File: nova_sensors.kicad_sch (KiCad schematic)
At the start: 93 parts, among them J1 Conn_01x03_Socket, J10 Conn_01x04_Socket, J11 Conn_01x04_Socket, J2 Conn_01x03_Socket, J3 Conn_01x04_Socket, J4 Conn_01x02_Socket, J5 Conn_01x02_Socket, J6 Conn_01x03_Socket, J7 Conn_01x02_Socket, J8 Conn_01x02_Socket, J9 Conn_01x02_Socket, SW1 SW_Push, SW2 SW_DIP_x02, SW3 SW_DIP_x02, U1 AT32F455CET7, U2 MAX3232, U3 MAX13488EESA+T, U4 MAX13488EESA+T, U5 LD1117S33TR, U6 XL1509-ADJ, Y1 8Mhz, Y2 32768hz

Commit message: refact: 调整丝印与网络标签，更新AT32 WorkBench配置
- PCB: 调整ADC1丝印位置并取消锁定
- SCH: 网络标签重命名 ADC_IN0->ADC1, ADC_IN1->ADC2
- ATWP: 工程重命名为nova_sensors，新增WDT/TMR1/DMA及串口中断等外设配置
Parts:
- J8: 定义 ADC_IN0 -> ADC1
- J9: 定义 ADC_IN1 -> ADC2
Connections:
- net ADC_IN0 renamed ADC1
- net ADC_IN1 renamed ADC2
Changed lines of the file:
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@@
 		)
 	)
-	(label "ADC_IN1"
+	(label "ADC2"
 		(at 33.02 88.9 0)
 		(effects
@@
 		)
 	)
-	(label "ADC_IN1"
+	(label "ADC2"
 		(at 218.44 228.6 0)
 		(effects
@@
 		)
 	)
-	(label "ADC_IN0"
+	(label "ADC1"
 		(at 250.19 228.6 0)
 		(effects
@@
 		)
 	)
-	(label "ADC_IN0"
+	(label "ADC1"
 		(at 33.02 86.36 0)
 		(effects
@@
 		)
 		(pin "19"
-			(alternate "ADC1_IN9")
+			(alternate "ADC2_IN9")
 		)
 		(pin "22"
@@
 			)
 		)
-		(property "定义" "ADC_IN1"
-			(at 241.3 231.14 0)
+		(property "定义" "ADC2"
+			(at 239.522 231.14 0)
 			(show_name no)
 			(do_not_autoplace no)
@@
 			)
 		)
-		(property "定义" "ADC_IN0"
-			(at 273.05 231.14 0)
+		(property "定义" "ADC1"
+			(at 271.272 231.14 0)
 			(show_name no)
 			(do_not_autoplace no)

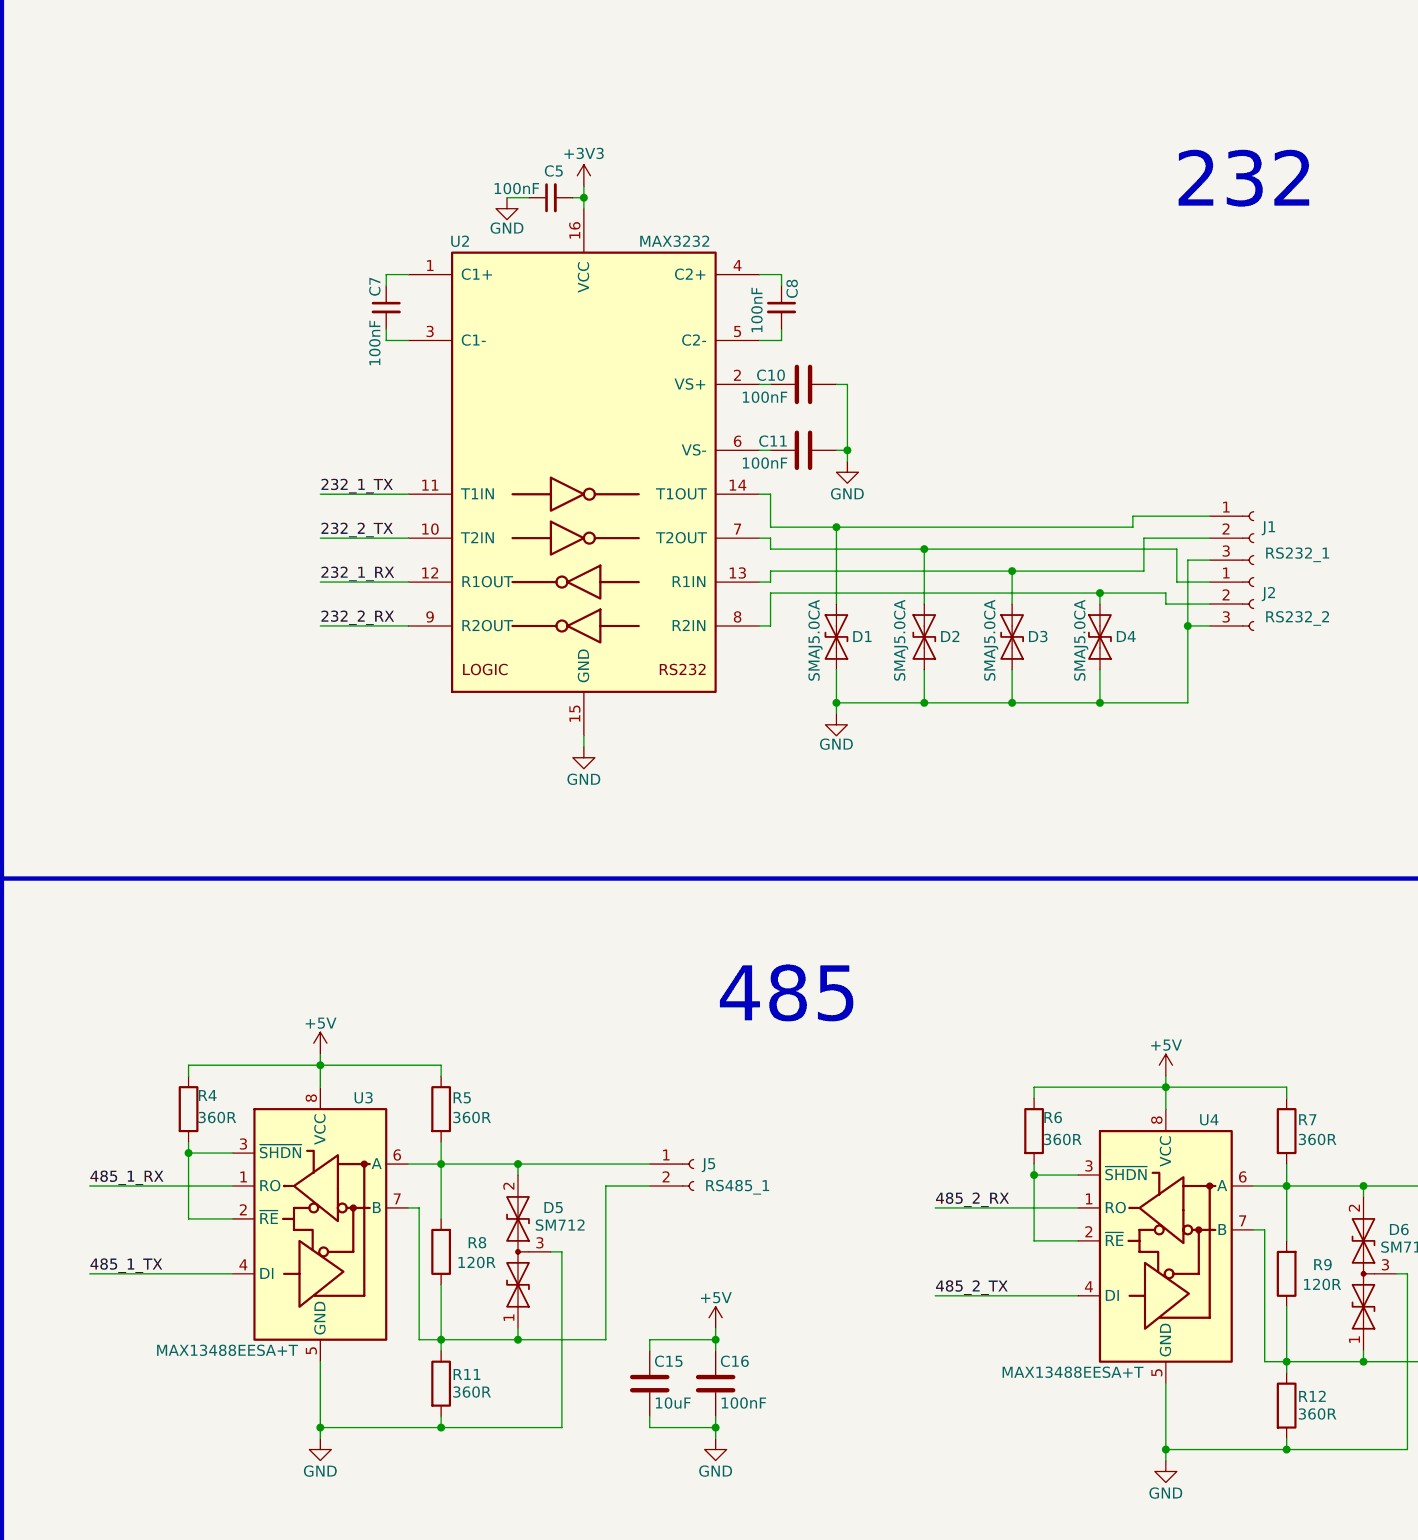
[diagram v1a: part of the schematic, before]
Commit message: fix: 修复工程专用符号库中485芯片缺失的问题，同时调整了485芯片的封装并更新了pcb
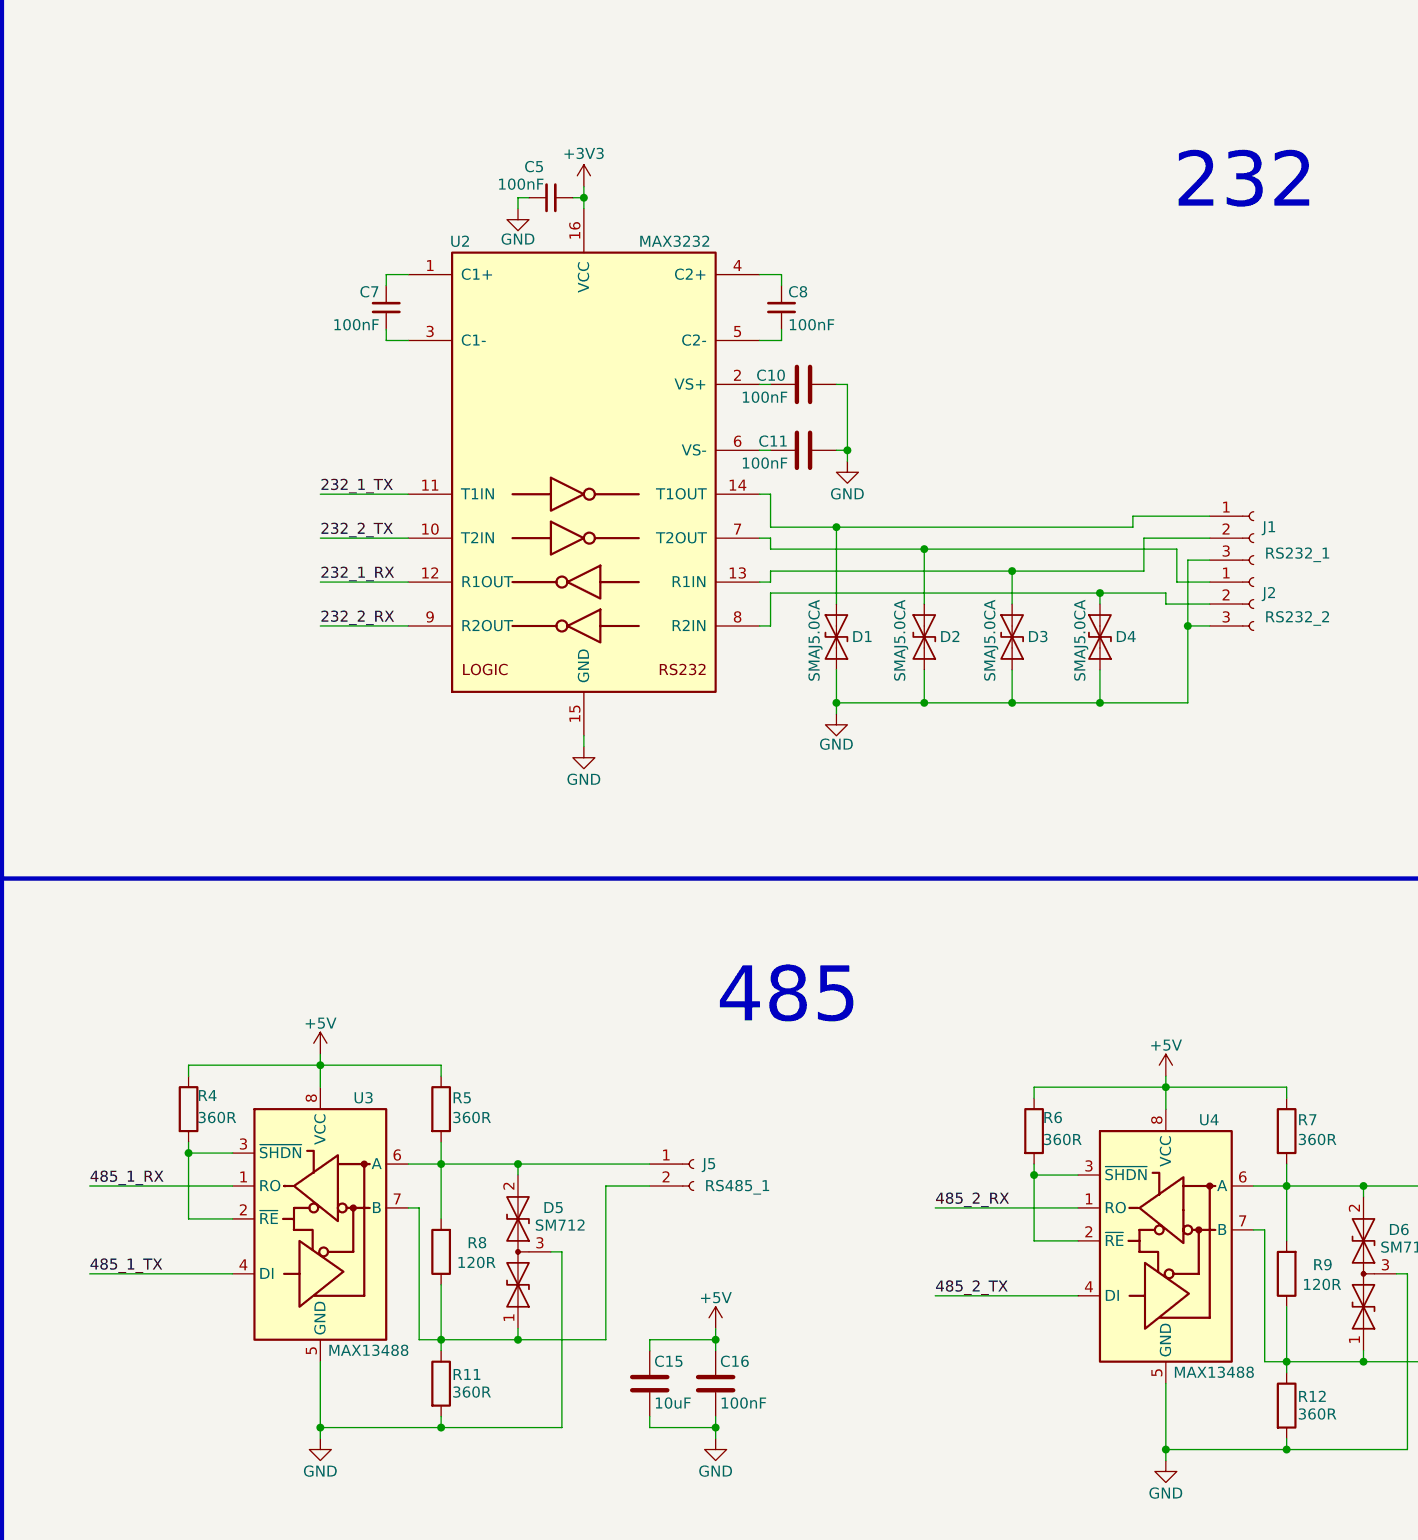
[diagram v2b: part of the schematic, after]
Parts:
- U3, U4: value MAX13488EESA+T -> MAX13488; footprint Package_SO:SSOP-8_3.95x5.21x3.27mm_P1.27mm -> Package_SO:SOIC-8_3.9x4.9mm_P1.27mm; symbol wyh:MAX13487EESA+T -> nova_sensors:MAX13488EESA+T

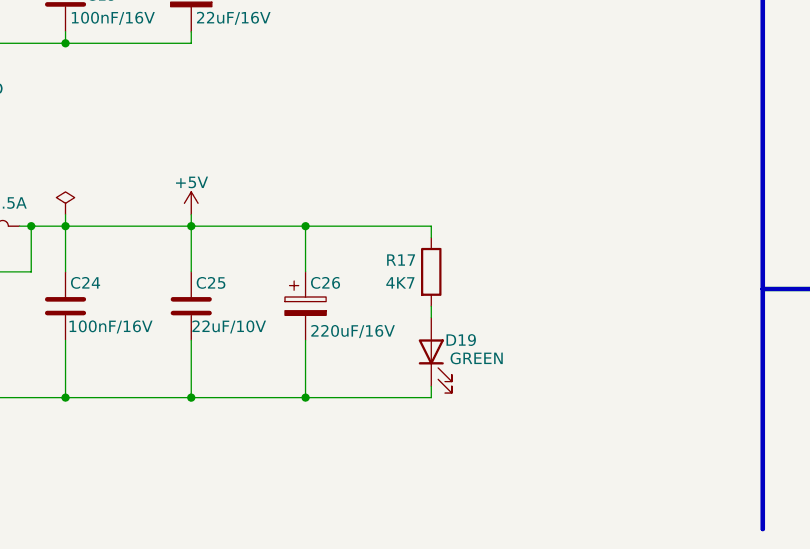
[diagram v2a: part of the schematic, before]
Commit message: fix: 调整电源指示灯的限流电阻大小，使其与其他两个灯亮度相近；调整装配图的说明文字位置，使其易于辨认
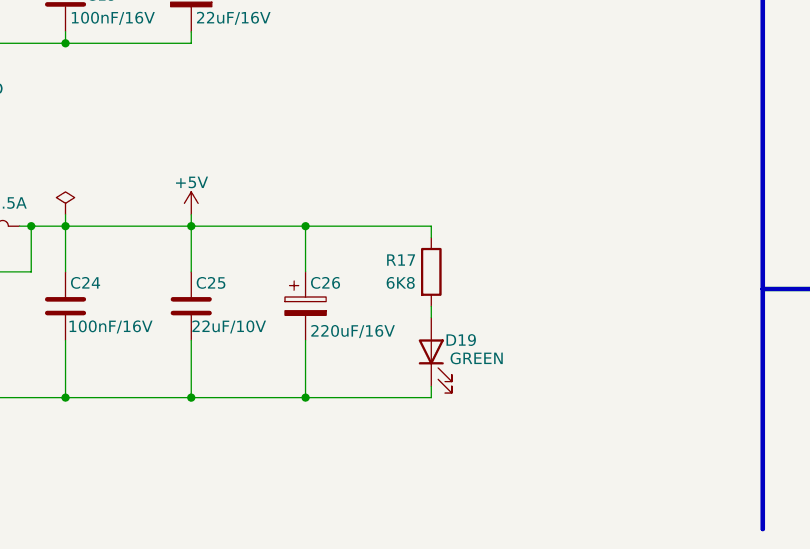
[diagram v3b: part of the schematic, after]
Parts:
- R17: value 4K7 -> 6K8
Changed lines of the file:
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@@
 			)
 		)
-		(property "Value" "4K7"
+		(property "Value" "6K8"
 			(at 162.56 257.81 0)
 			(show_name no)

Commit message: fix: 微调丝印位置
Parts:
- D1, D2, D3, D4: footprint Diode_SMD:D_SMB -> Diode_SMD:D_SMA
- D10, D11, D12, D13, D14, D15, D16, D17: footprint Diode_SMD:D_SMA-SMB_Universal_Handsoldering -> Diode_SMD:D_SMA
- U2: footprint Package_SO:SOIC-16W_5.3x10.2mm_P1.27mm -> Package_SO:SOIC-16_3.9x9.9mm_P1.27mm
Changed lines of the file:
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@@
 			)
 		)
-		(property "Footprint" "Diode_SMD:D_SMA-SMB_Universal_Handsoldering"
+		(property "Footprint" "Diode_SMD:D_SMA"
 			(at 304.8 236.22 0)
 			(hide yes)
@@
 			)
 		)
-		(property "Footprint" "Diode_SMD:D_SMA-SMB_Universal_Handsoldering"
+		(property "Footprint" "Diode_SMD:D_SMA"
 			(at 259.08 233.68 0)
 			(hide yes)
@@
 			)
 		)
-		(property "Footprint" "Diode_SMD:D_SMA-SMB_Universal_Handsoldering"
+		(property "Footprint" "Diode_SMD:D_SMA"
 			(at 295.91 236.22 0)
 			(hide yes)
@@
 			)
 		)
-		(property "Footprint" "Diode_SMD:D_SMB"
+		(property "Footprint" "Diode_SMD:D_SMA"
 			(at 316.23 92.71 0)
 			(hide yes)
@@
 			)
 		)
-		(property "Footprint" "Diode_SMD:D_SMA-SMB_Universal_Handsoldering"
+		(property "Footprint" "Diode_SMD:D_SMA"
 			(at 313.69 236.22 0)
 			(hide yes)
@@
 			)
 		)
-		(property "Footprint" "Diode_SMD:D_SMB"
+		(property "Footprint" "Diode_SMD:D_SMA"
 			(at 326.39 92.71 0)
 			(hide yes)
@@
 			)
 		)
-		(property "Footprint" "Diode_SMD:D_SMA-SMB_Universal_Handsoldering"
+		(property "Footprint" "Diode_SMD:D_SMA"
 			(at 346.71 236.22 0)
 			(hide yes)
@@
 			)
 		)
-		(property "Footprint" "Diode_SMD:D_SMA-SMB_Universal_Handsoldering"
+		(property "Footprint" "Diode_SMD:D_SMA"
 			(at 227.33 233.68 0)
 			(hide yes)
@@
 			)
 		)
-		(property "Footprint" "Diode_SMD:D_SMA-SMB_Universal_Handsoldering"
+		(property "Footprint" "Diode_SMD:D_SMA"
 			(at 364.49 236.22 0)
 			(hide yes)
@@
 			)
 		)
-		(property "Footprint" "Package_SO:SOIC-16W_5.3x10.2mm_P1.27mm"
+		(property "Footprint" "Package_SO:SOIC-16_3.9x9.9mm_P1.27mm"
 			(at 273.05 100.33 0)
 			(hide yes)
@@
 			)
 		)
-		(property "Footprint" "Diode_SMD:D_SMB"
+		(property "Footprint" "Diode_SMD:D_SMA"
 			(at 336.55 92.71 0)
 			(hide yes)
@@
 			)
 		)
-		(property "Footprint" "Diode_SMD:D_SMA-SMB_Universal_Handsoldering"
+		(property "Footprint" "Diode_SMD:D_SMA"
 			(at 355.6 236.22 0)
 			(hide yes)
@@
 			)
 		)
-		(property "Footprint" "Diode_SMD:D_SMB"
+		(property "Footprint" "Diode_SMD:D_SMA"
 			(at 306.07 92.71 0)
 			(hide yes)

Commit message: fix: 调整贴片铝解电容的封装大小
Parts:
- C26: footprint Capacitor_SMD:CP_Elec_8x10 -> Capacitor_SMD:CP_Elec_6.3x7.7
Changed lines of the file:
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@@
 			)
 		)
-		(property "Footprint" "Capacitor_SMD:CP_Elec_8x10"
+		(property "Footprint" "Capacitor_SMD:CP_Elec_6.3x7.7"
 			(at 154.6352 264.16 0)
 			(hide yes)
